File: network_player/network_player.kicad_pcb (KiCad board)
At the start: 4 copper layers, 30.1 x 66.6 mm, 76 parts, among them J1 Raspberry_Pi_2_3, J4 USB_C_Receptacle_USB2.0, Q1 BC817, Q2 BC817, Q3 MMBT3904, SW1 SW_Push, SW2 SW_Push, SW3 SW_Push, U1 F1C100s, U3 W25N01GVZEIG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

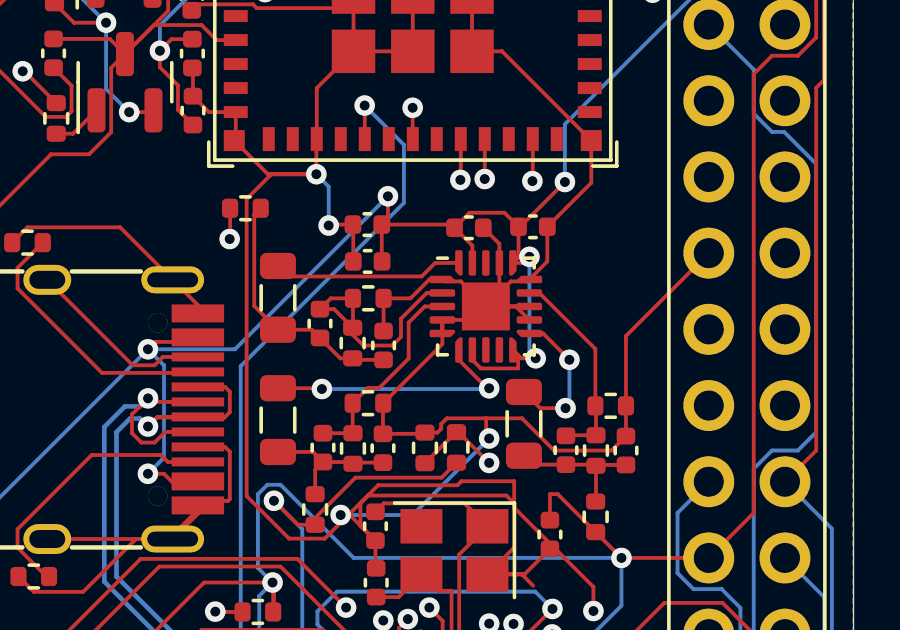
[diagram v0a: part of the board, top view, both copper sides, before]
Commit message: Change footprint of EA3036 and generate gerbers + drill files
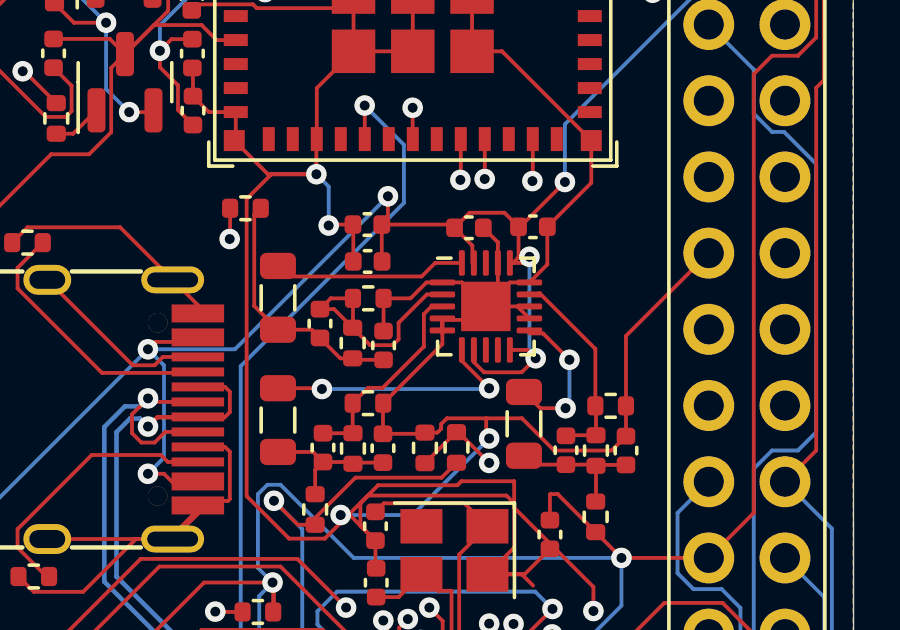
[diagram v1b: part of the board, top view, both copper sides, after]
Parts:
- C22, C23: value 30pF -> 33pF
- U6: footprint Package_DFN_QFN:QFN-20-1EP_3x3mm_P0.45mm_EP1.6x1.6mm -> Package_DFN_QFN:QFN-20-1EP_3x3mm_P0.4mm_EP1.65x1.65mm
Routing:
- net GND: track 378.6 -> 377.2 mm
- net +5V: track 80.6 -> 81.1 mm

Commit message: Fully update gerbers before sending again to jlcpcb, also add silkscreen with copyright
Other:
- board text added: "Aguirre N. (c) 2024"
- board text added: "La Manufacture du Son Network player v1.0"
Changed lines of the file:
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@@
   (gr_arc (start 105.4354 46.7868) (mid 106.304268 44.651197) (end 108.432494 43.764414)
     (stroke (width 0.0381) (type default)) (layer "Edge.Cuts"))
+  (gr_text "La Manufacture du Son\nNetwork player v1.0" (at 129.13 105.86) (layer "B.SilkS")
+    (effects (font (size 1 1) (thickness 0.25) bold) (justify left bottom mirror))
+  )
+  (gr_text "Aguirre N.\n(c) 2024" (at 126.27 47.32) (layer "B.SilkS")
+    (effects (font (size 1.524 1.524) (thickness 0.3048) bold) (justify left bottom mirror))
+  )
   (segment (start 107.46 92.35) (end 107.46 90.885) (width 0.127) (layer "F.Cu") (net 1))
   (segment (start 113.69 65.33) (end 112.27 65.33) (width 0.127) (layer "F.Cu") (net 1))

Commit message: first corrections
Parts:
- added R23: 10k, Resistor_SMD:R_0402_1005Metric, F.Cu at (98.5, 70.7)
- added R24: 10k, Resistor_SMD:R_0402_1005Metric, F.Cu at (98.5, 72.7)
- added R25: 0R, Resistor_SMD:R_0402_1005Metric, F.Cu at (98.5, 74.7)
- added R26: 0R, Resistor_SMD:R_0402_1005Metric, F.Cu at (98.5, 76.7)
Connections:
- J1 pad 13: unconnected-(J1-GPIO27-Pad13) -> /ESP32_USB_D-
- J1 pad 16: /U0TXD -> /ESP32_TX
- J1 pad 18: /U0RXD -> /ESP32_RX
- J1 pad 22: /DTR -> /ESP32_USB_D+
- J1 pad 37: /RTS -> /SPDIF
- J1 pad 38: /SPDIF -> /I2S_DIN
- U1 pad 10: /U0RXD -> /ESP32_RXD
- U1 pad 44: unconnected-(U1A-PE5/CSI_D2/LCD_D17/DA_IN/EINTE5-Pad44) -> /I2S_DIN
- U1 pad 9: /U0TXD -> /ESP32_TXD
- U4 pad 22: unconnected-(U4-GPIO8-Pad22) -> /GPIO_8
- U4 pad 26: unconnected-(U4-GPIO18/USB_D--Pad26) -> /ESP32_USB_D-
- U4 pad 27: unconnected-(U4-GPIO19/USB_D+-Pad27) -> /ESP32_USB_D+
- U4 pad 30: /U0RXD -> /ESP32_RX
- U4 pad 31: /U0TXD -> /ESP32_TX
- U6 pad 18: unconnected-(U6-EN3-Pad18) -> +5V
- U6 pad 8: unconnected-(U6-EN2-Pad8) -> +5V
- U6 pad 9: unconnected-(U6-EN1-Pad9) -> +5V
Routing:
- net /U0TXD: track 80.1 -> 0.00 mm, vias 1 -> 0
- net /U0RXD: track 72.2 -> 0.00 mm, vias 2 -> 0
- net /DTR: track 102.3 -> 42.6 mm
- net /SPDIF: track 17.5 -> 0.00 mm
- net /RTS: track 67.6 -> 54.1 mm

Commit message: recover for v1.1
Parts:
- removed Q1, Q2: BC817, Package_TO_SOT_SMD:SOT-23
- removed R11, R12, R26: 0R, Resistor_SMD:R_0402_1005Metric
- removed R14, R15: 10k, Resistor_SMD:R_0402_1005Metric
- R25: value 0R -> 10k
- moved R25 32.6 mm to (119.1, 100.0), turned to 180 degrees
- moved R24 27.3 mm to (122.9, 60.3), turned to 180 degrees
- moved R23 25.4 mm to (113.0, 49.8), turned to 180 degrees
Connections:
- net /GPIO_8 renamed Net-(U4-GPIO8)
- C33 pad 1: /CHIP_PU -> /ESP_RST
- J1 pad 12: /GPIO18 -> unconnected-(J1-GPIO18/PWM0-Pad12)
- J1 pad 13: /ESP32_USB_D- -> unconnected-(J1-GPIO27-Pad13)
- J1 pad 16: /ESP32_TX -> /U0TXD
- J1 pad 18: /ESP32_RX -> /U0RXD
- J1 pad 22: /ESP32_USB_D+ -> /DTR
- J1 pad 23: /SPI_CLK -> /SPI_MCLK
- J1 pad 37: /SPDIF -> /RTS
- J1 pad 38: /I2S_DIN -> /SPDIF
- R13 pad 2: /CHIP_PU -> /ESP_RST
- R23 pad 1: /GPIO_9 -> +3V3
- R23 pad 2: +3V3 -> /WIFI_HANDSHAKE
- R24 pad 2: +3V3 -> GND
- R25 pad 1: /ESP32_RX -> +3V3
- R25 pad 2: /ESP32_TXD -> /ESP_BOOT
- SW2 pad 1: /GPIO_9 -> /SPI_MOSI
- SW3 pad 1: /CHIP_PU -> /ESP_RST
- U1 pad 10: /ESP32_RXD -> /U0RXD
- U1 pad 26: /WIFI_SPI_CS -> /SPI_CS
- U1 pad 27: /WIFI_SPI_MOSI -> unconnected-(U1A-PD19/LCD_DE/SPI0_MOSI/EINTD19-Pad27)
- U1 pad 28: /WIFI_SPI_CLK -> unconnected-(U1A-PD20/LCD_HSYNC/SPI0_CLK/EINTD20-Pad28)
- U1 pad 29: /WIFI_SPI_MISO -> unconnected-(U1A-PD21/LCD_VSYNC/SPI0_MISO/EINTD21-Pad29)
- U1 pad 39: /SPI_MISO -> /WIFI_SPI_MISO
- U1 pad 40: /SPI_CLK -> /WIFI_SPI_CLK
- U1 pad 41: /SPI_MOSI -> /WIFI_SPI_MOSI
- U1 pad 42: /SPI_CS -> /WIFI_SPI_CS
- U1 pad 44: /I2S_DIN -> unconnected-(U1A-PE5/CSI_D2/LCD_D17/DA_IN/EINTE5-Pad44)
- U1 pad 59: Net-(U1A-PC0/SPI0_CLK/SDC1_CLK) -> /SPI_MCLK
- U1 pad 61: Net-(U1A-PC2/SPI0_MISO/SDC1_D0) -> /SPI_MISO
- U1 pad 62: Net-(U1A-PC3/SPI0_MOSI/UART0_TX) -> /SPI_MOSI
- U1 pad 7: /DTR -> /ESP_RST
- U1 pad 79: /GPIO18 -> unconnected-(U1A-LRADC0-Pad79)
- U1 pad 8: /RTS -> /ESP_BOOT
- U1 pad 9: /ESP32_TXD -> /U0TXD
- U3 pad 2: Net-(U1A-PC2/SPI0_MISO/SDC1_D0) -> /SPI_MISO
- U3 pad 5: Net-(U1A-PC3/SPI0_MOSI/UART0_TX) -> /SPI_MOSI
- U3 pad 6: Net-(U1A-PC0/SPI0_CLK/SDC1_CLK) -> /SPI_MCLK
- U4 pad 23: /GPIO_9 -> /ESP_BOOT
- U4 pad 26: /ESP32_USB_D- -> unconnected-(U4-GPIO18/USB_D--Pad26)
- U4 pad 27: /ESP32_USB_D+ -> unconnected-(U4-GPIO19/USB_D+-Pad27)
- U4 pad 30: /ESP32_RX -> /U0RXD
- U4 pad 31: /ESP32_TX -> /U0TXD
- U4 pad 8: /CHIP_PU -> /ESP_RST
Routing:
- net /SPI_MISO: track 5.75 -> 157.8 mm, vias 1 -> 3
- net /ESP_BOOT: track 0.00 -> 110.7 mm, vias 0 -> 3
- net /ESP_RST: track 0.00 -> 99.7 mm, vias 0 -> 2
- net /GPIO_9: track 90.3 -> 0.00 mm, vias 4 -> 0
- net /SPI_MOSI: track 6.70 -> 91.5 mm, vias 1 -> 7
- net /U0TXD: track 0.00 -> 80.1 mm, vias 0 -> 1
- net /CHIP_PU: track 72.2 -> 0.00 mm
- net /U0RXD: track 0.00 -> 72.2 mm, vias 0 -> 2
- net /SPI_MCLK: track 0.00 -> 71.3 mm, vias 0 -> 4
- net /GPIO18: track 60.0 -> 0.00 mm, vias 1 -> 0
- net /RTS: track 54.1 -> 0.00 mm, vias 2 -> 0
- net /DTR: track 42.6 -> 93.8 mm, vias 2 -> 0
- net Net-(U1A-PC2/SPI0_MISO/SDC1_D0): track 30.7 -> 0.00 mm, vias 2 -> 0
- net Net-(Q1-C): track 18.9 -> 0.00 mm, vias 3 -> 0
- net Net-(U1A-PC0/SPI0_CLK/SDC1_CLK): track 17.5 -> 0.00 mm
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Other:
- board text added: "BS"
- board text added: "ESP_RST"
- board text added: "La Manufacture Du Son Network Player v1.1"
- board text added: "RST"
- board text removed: "La Manufacture du Son Network player v1.0"
